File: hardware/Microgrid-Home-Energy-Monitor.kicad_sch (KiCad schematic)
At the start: 11 parts, among them U1 ESP32-WROOM-32, U2 MCP6002-xP, U3 MCP6002-xP

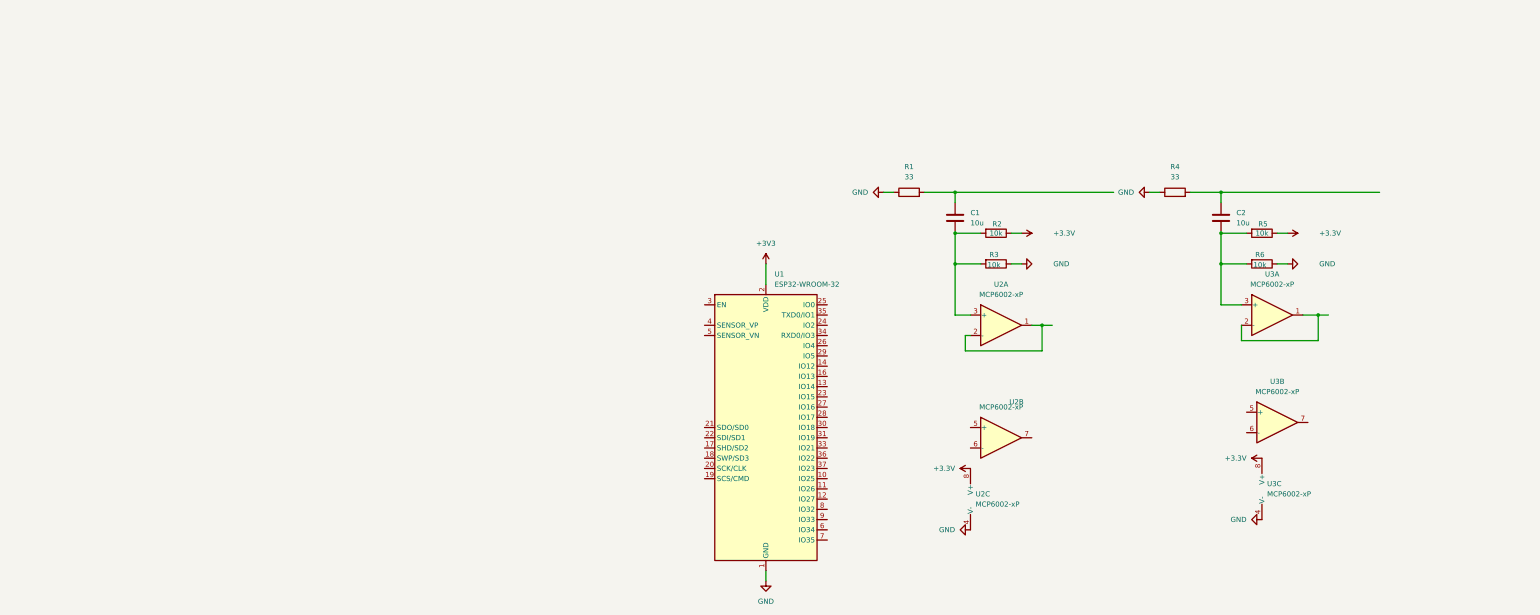
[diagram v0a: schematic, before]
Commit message: add OLED connector, USB-C power input, AMS1117 regulator, decoupling caps
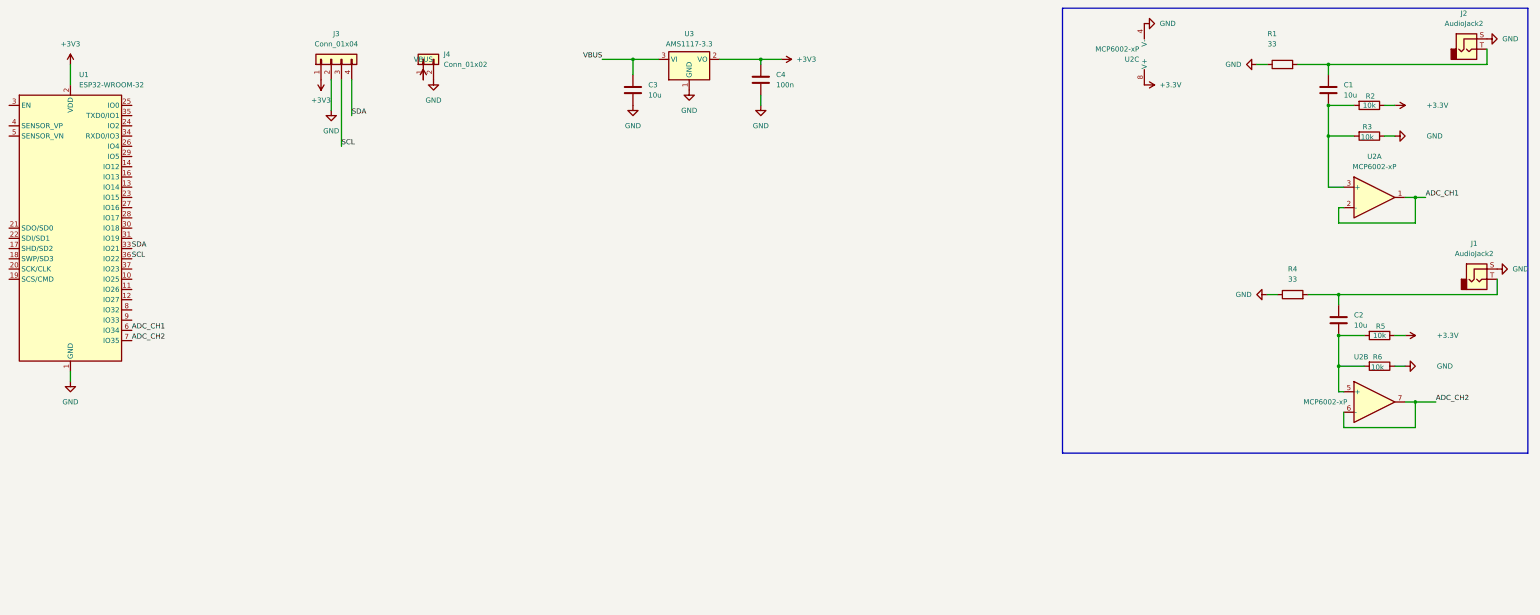
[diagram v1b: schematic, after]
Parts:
- removed U3: MCP6002-xP, symbol Amplifier_Operational:MCP6002-xP
- added C3: 10u, symbol Device:C
- added C4: 100n, symbol Device:C
- added J1, J2: AudioJack2, symbol Connector_Audio:AudioJack2
- added J3: Conn_01x04, symbol Connector_Generic:Conn_01x04
- added J4: Conn_01x02, symbol Connector_Generic:Conn_01x02
- added U3: AMS1117-3.3, Package_TO_SOT_SMD:SOT-223-3_TabPin2, symbol Regulator_Linear:AMS1117-3.3
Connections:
- net +3V3: now also C4.1, J3.1 (Pin_1), U3.2 (VO)
- net GND: now also C3.2, C4.2, J1.S, J2.S, J3.2 (Pin_2), J4.2 (Pin_2), U3.1 (GND)
- net at C2.1, R4.2: now also J1.T
- net at C2.2, R5.2, R6.2: now also U2.5 (+)
- net at C1.1, R1.2: now also J2.T
- net ADC_CH1: now reaches U2.1, U2.2 (-)
- net ADC_CH1: now also U1.6 (IO34)
- net SDA: now reaches U1.33 (IO21)
- net SDA: now also J3.4 (Pin_4)
- net SCL: now reaches U1.36 (IO22)
- net SCL: now also J3.3 (Pin_3)
- net ADC_CH2: now reaches U1.7 (IO35)
- net ADC_CH2: now also U2.6 (-), U2.7
- new net VBUS: C3.1, J4.1 (Pin_1), U3.3 (VI)
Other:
- moved on the sheet: C1, R1, R2, R3, U1, U2A, U2B, U2C

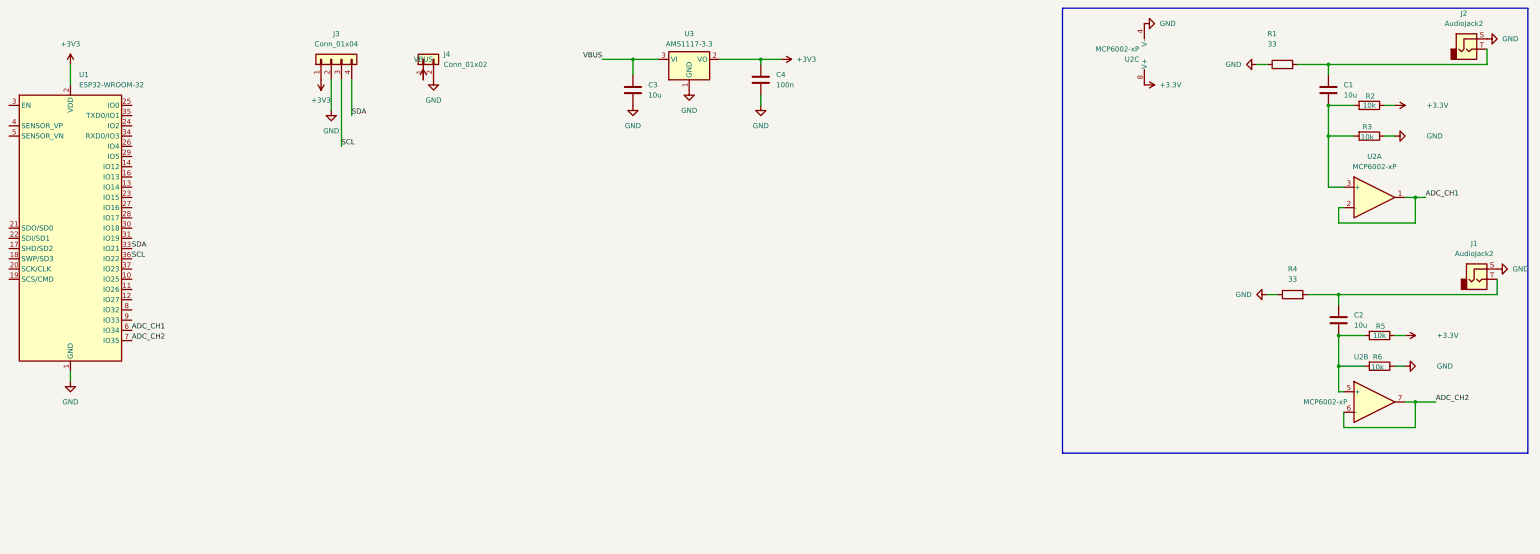
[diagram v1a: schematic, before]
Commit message: complete schematic — ERC clean, all components wired
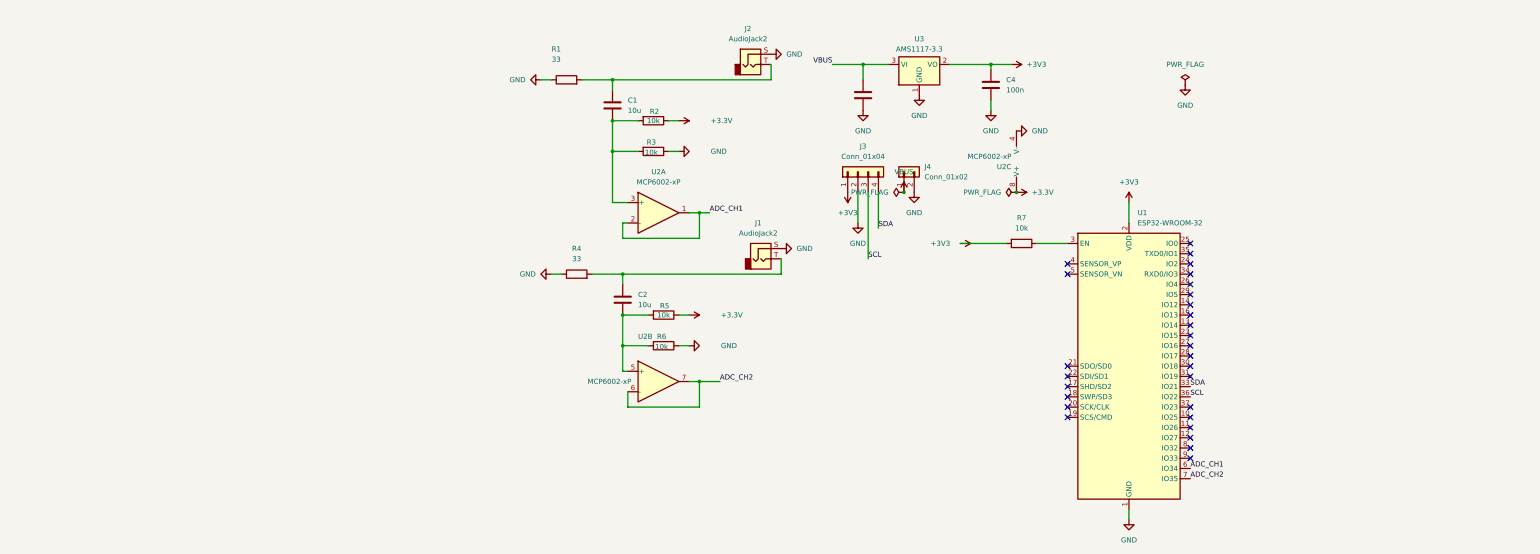
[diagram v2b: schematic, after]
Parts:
- added R7: 10k, symbol Device:R
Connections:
- net +3V3: now also R7.2
- net at U1.3 (EN): now also R7.1
- no-connect marks 0 -> 28
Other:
- moved on the sheet: C1, C2, C4, J1, J2, J3, J4, R1, R2, R3, R4, R5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

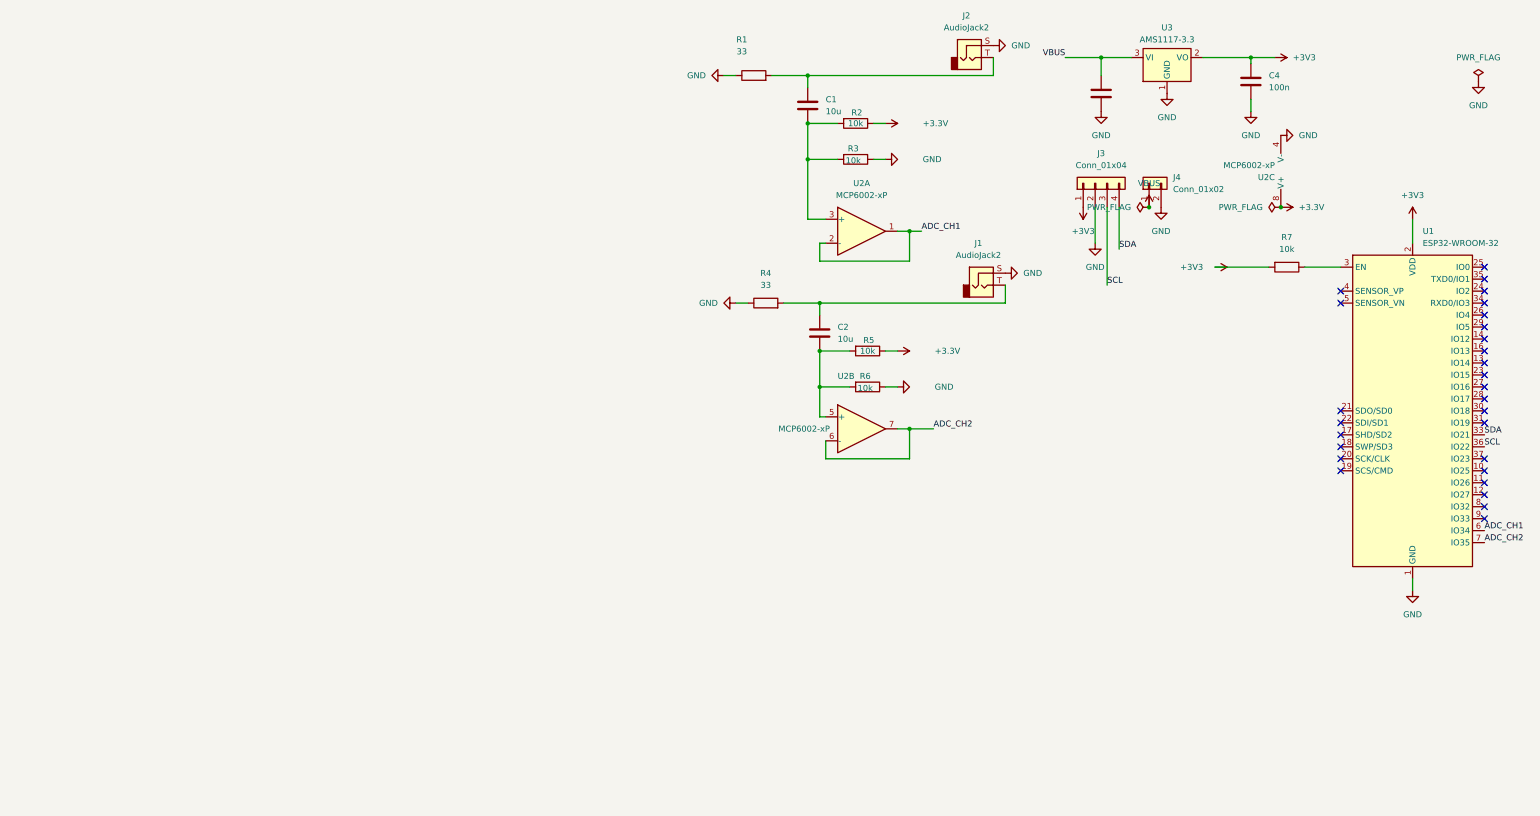
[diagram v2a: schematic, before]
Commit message: Complete schematic fixes: USB-C, decoupling caps, boot/reset buttons, I2C pullups, programming header, ZMPT101B connector
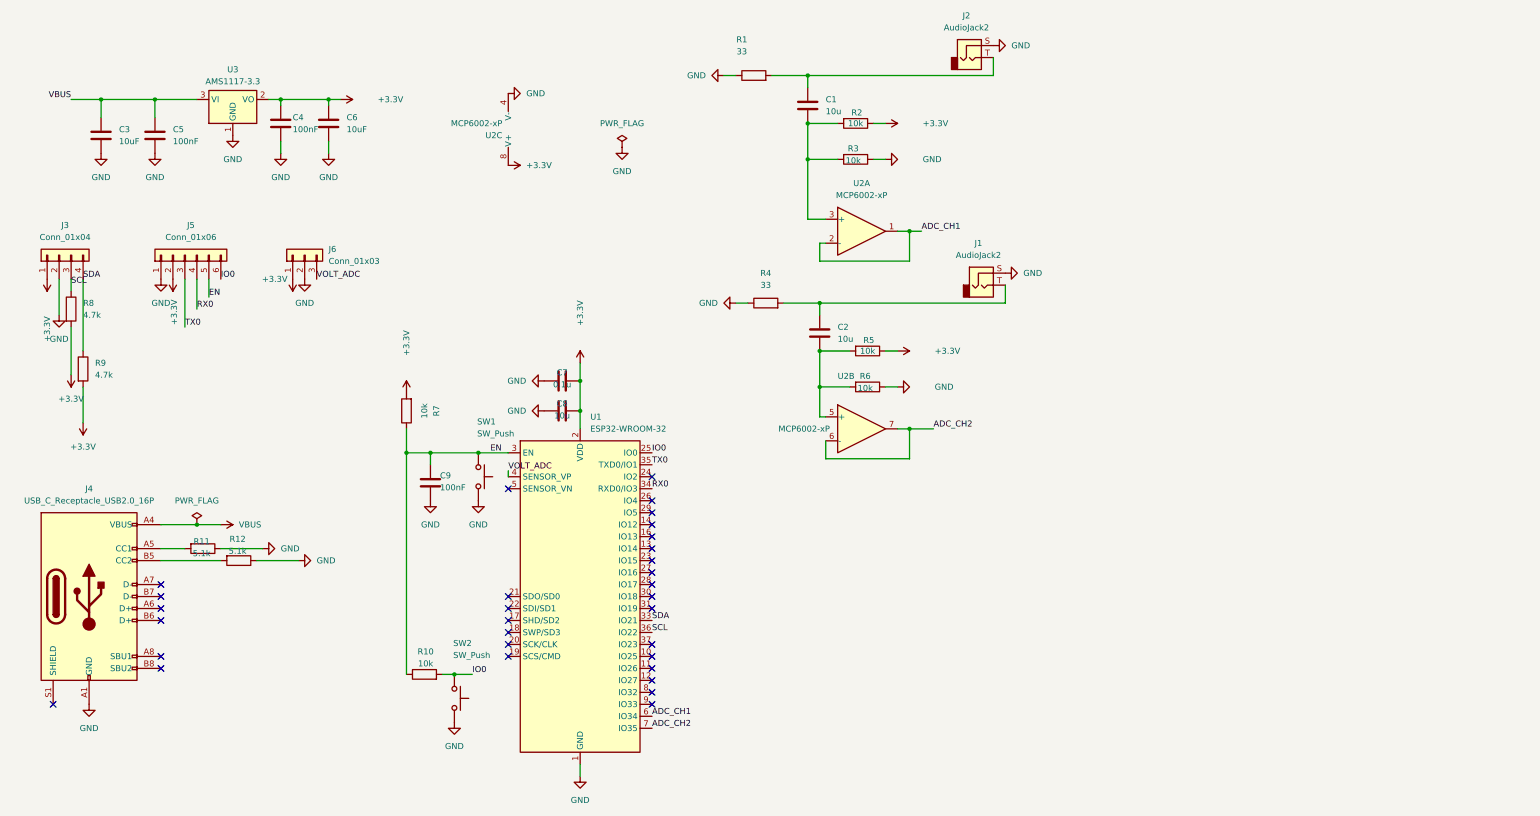
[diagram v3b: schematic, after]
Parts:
- removed J4: Conn_01x02, symbol Connector_Generic:Conn_01x02
- added C5, C9: 100nF, symbol Device:C
- added C6: 10uF, symbol Device:C
- added C7: 0.1u, symbol Device:C
- added C8: 10u, symbol Device:C
- added J4: USB_C_Receptacle_USB2.0_16P, symbol Connector:USB_C_Receptacle_USB2.0_16P
- added J5: Conn_01x06, symbol Connector_Generic:Conn_01x06
- added J6: Conn_01x03, symbol Connector_Generic:Conn_01x03
- added R10: 10k, symbol Device:R
- added R11, R12: 5.1k, symbol Device:R
- added R8, R9: 4.7k, symbol Device:R
- added SW1, SW2: SW_Push, symbol Switch:SW_Push
- C3: value 10u -> 10uF
- C4: value 100n -> 100nF
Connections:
- net +3V3 is gone; now on net +3.3V: C4.1, J3.1 (Pin_1), R7.2, U1.2 (VDD), U3.2 (VO)
- net +3.3V: now also C6.1, C7.2, C8.2, J5.2 (Pin_2), J6.1 (Pin_1), R8.2, R9.2
- net GND: now also C5.2, C6.2, C7.1, C8.1, C9.2, J4.A1 (GND), J4.A12 (GND), J4.B1 (GND), J4.B12 (GND), J5.1 (Pin_1), J6.2 (Pin_2), R11.1, R12.1, SW1.2, SW2.2
- net SCL: now also R8.1
- net SDA: now also R9.1
- net VBUS: now also C5.1, J4.A4 (VBUS), J4.A9 (VBUS), J4.B4 (VBUS), J4.B9 (VBUS)
- net EN: now reaches R7.1, U1.3 (EN)
- net EN: now also C9.1, J5.5 (Pin_5), R10.1, SW1.1
- net IO0: now reaches U1.25 (IO0)
- net IO0: now also J5.6 (Pin_6), R10.2, SW2.1
- net RX0: now reaches U1.34 (RXD0/IO3)
- net RX0: now also J5.4 (Pin_4)
- net TX0: now reaches U1.35 (TXD0/IO1)
- net TX0: now also J5.3 (Pin_3)
- net VOLT_ADC: now reaches U1.4 (SENSOR_VP)
- net VOLT_ADC: now also J6.3 (Pin_3)
- new net: J4.A5 (CC1), R11.2
- new net: J4.B5 (CC2), R12.2
- no-connect marks 28 -> 31
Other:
- moved on the sheet: C4, J3, R7, U1, U2C, U3
